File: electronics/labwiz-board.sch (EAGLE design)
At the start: 97 parts, among them J1 SD_MICRO_SDIO_1BIT, J2 CORTEX_DEBUGSMD_original, U1 STM32F10XRXT6, U2 MCP73831/2, U4 MIC5219-3.3V, X2 M12_BOTTOM_CONTACTS_FPC_1MM, Y3 32.768kHz

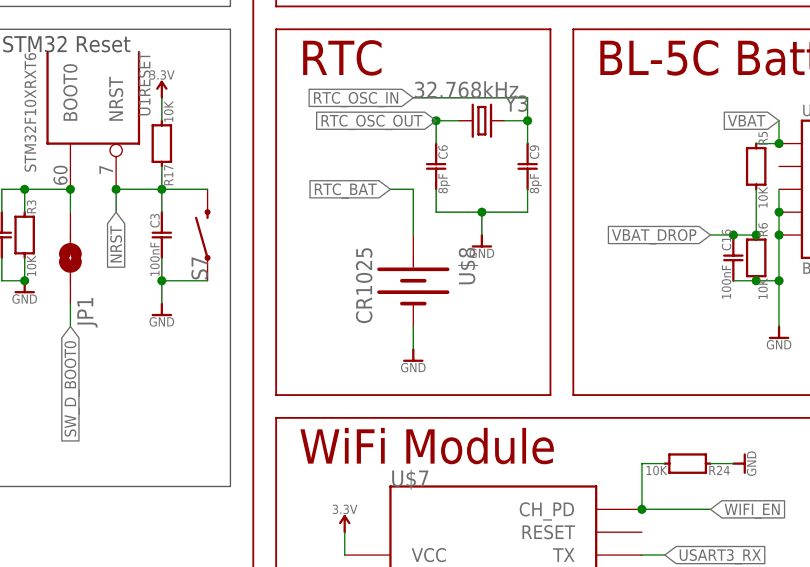
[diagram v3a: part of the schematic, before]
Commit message: Routed the RTC battery. Bumped a bunch of traces around.
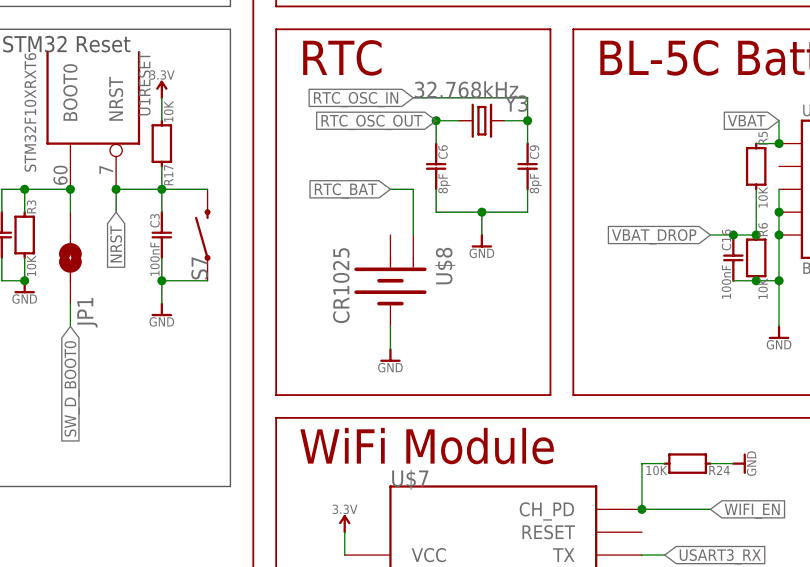
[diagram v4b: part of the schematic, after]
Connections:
- net RTC_BAT: now also U$8.+1; no longer U$8.+
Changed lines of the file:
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@@
 <instance part="C6" gate="G$1" x="132.08" y="73.66" rot="R180"/>
 <instance part="C9" gate="G$1" x="142.24" y="73.66" rot="R180"/>
-<instance part="GND5" gate="G$1" x="129.54" y="53.34"/>
+<instance part="GND5" gate="G$1" x="127" y="53.34"/>
 <instance part="U$2" gate="G$1" x="342.9" y="15.24"/>
 <instance part="R18" gate="G$1" x="269.24" y="25.4" rot="MR90"/>
@@
 <instance part="SUPPLY10" gate="G$1" x="121.92" y="33.02"/>
 <instance part="TP1" gate="G$1" x="116.84" y="27.94" rot="R180"/>
-<instance part="U$8" gate="G$1" x="129.54" y="60.96" rot="R270"/>
+<instance part="U$8" gate="G$1" x="127" y="60.96"/>
 </instances>
 <busses>
@@
 <pinref part="GND5" gate="G$1" pin="GND"/>
 <pinref part="U$8" gate="G$1" pin="-"/>
-<wire x1="129.54" y1="53.34" x2="129.54" y2="55.88" width="0.1524" layer="91"/>
+<wire x1="127" y1="53.34" x2="127" y2="55.88" width="0.1524" layer="91"/>
 </segment>
 <segment>
@@
 </segment>
 <segment>
-<wire x1="129.54" y1="66.04" x2="129.54" y2="71.12" width="0.1524" layer="91"/>
 <wire x1="129.54" y1="71.12" x2="127" y2="71.12" width="0.1524" layer="91"/>
-<pinref part="U$8" gate="G$1" pin="+"/>
-</segment>
-</net>
+<pinref part="U$8" gate="G$1" pin="+1"/>
+<wire x1="129.54" y1="71.12" x2="129.54" y2="66.04" width="0.1524" layer="91"/>
+</segment>
+</net>

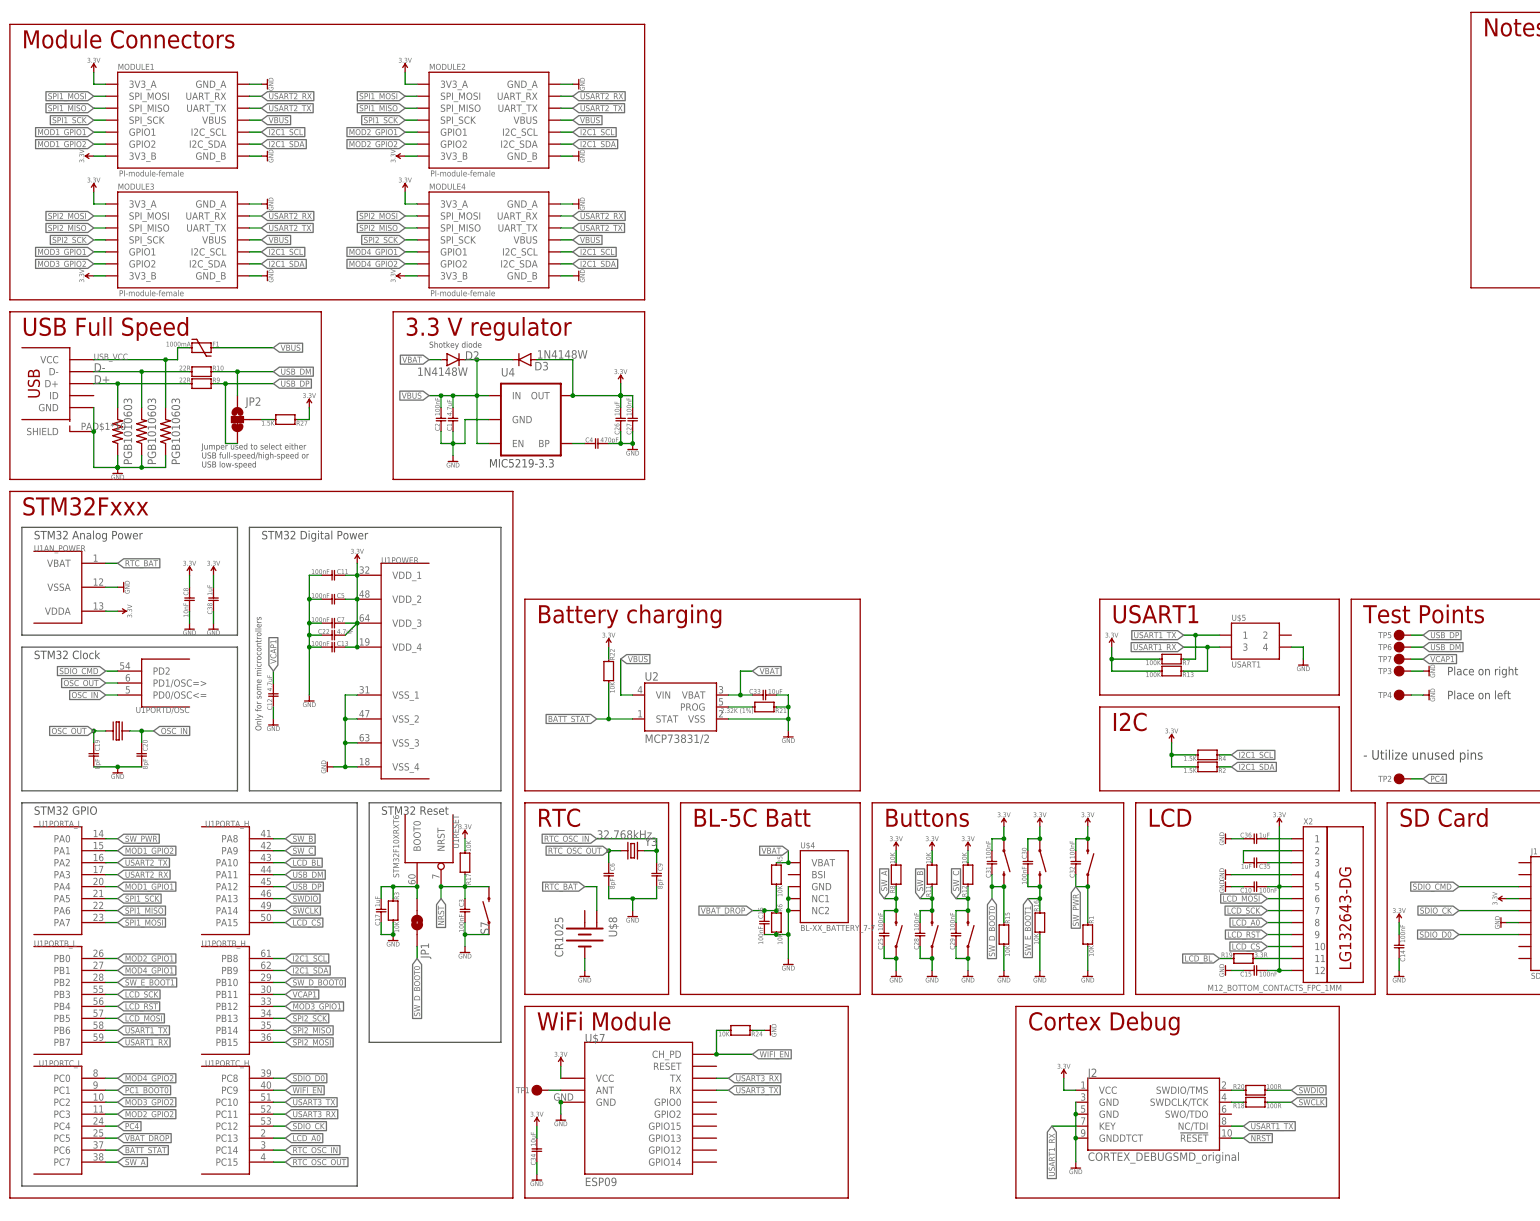
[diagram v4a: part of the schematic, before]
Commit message: PC4 is now VBUS_DETECT. Removed unnecessary USB data series resistors. Closes #76.'
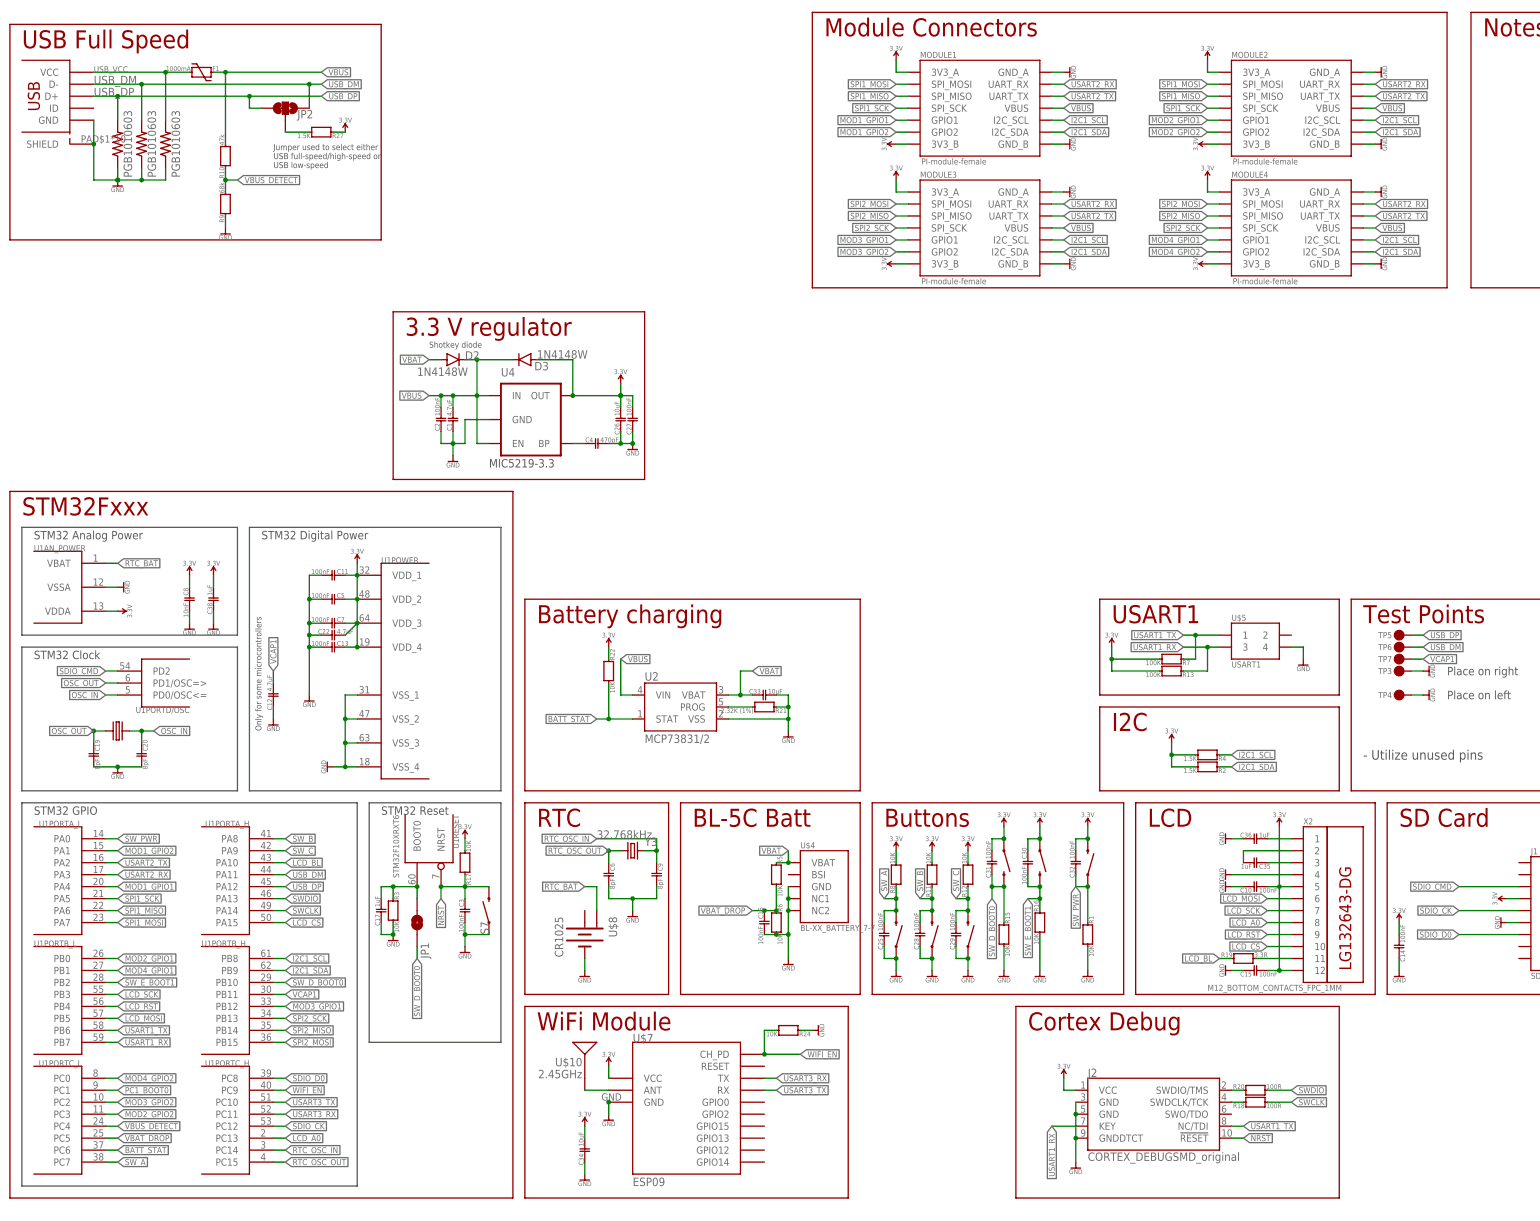
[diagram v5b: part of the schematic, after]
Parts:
- removed TP1, TP2: DNP, PaxInstruments-Connectors:M01_PAD_1MM
- added U$10: 2.45GHz, SparkFun-RF:ANTENNA2.4GHZ-6.5X2.2MM
- R10: value 22R -> 47k; device PaxInstruments-RCL:RESISTOR_FIXED_22R_0402 -> PaxInstruments-RCL:RESISTOR_FIXED_0402
- R9: value 22R -> 68k; device PaxInstruments-RCL:RESISTOR_FIXED_22R_0402 -> PaxInstruments-RCL:RESISTOR_FIXED_0402
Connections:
- removed net D+: R9.1, U$1.D+, Z1.2
- removed net D-: R10.1, U$1.D-, Z2.2
- removed net PC4: TP2.P$1, U1PORTC_L.PC4
- new net VBUS_DETECT: R10.2, R9.1, U1PORTC_L.PC4
- net GND: now also R9.2
- net N$13: now also U$10.SIGNAL; no longer TP1.P$1
- net USB_DM: now also U$1.D-, Z2.2; no longer R10.2
- net USB_DP: now also U$1.D+, Z1.2; no longer R9.2
- net VBUS: now also R10.1
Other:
- moved on the sheet: C34, F1, JP2, MODULE1, MODULE2, MODULE3, MODULE4, R10, R24, R27, R9, U$7

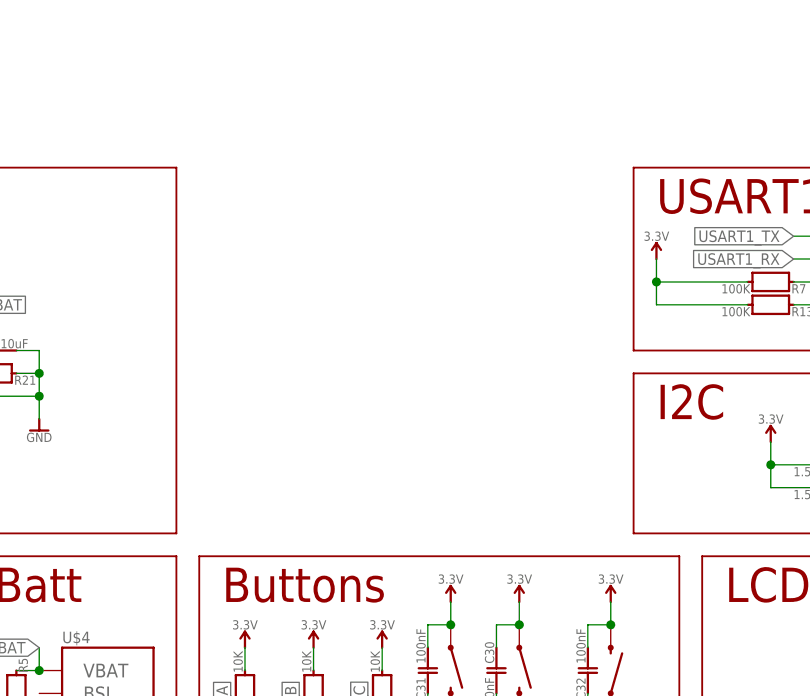
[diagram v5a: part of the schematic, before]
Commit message: Added SPI pullups. Need to route.
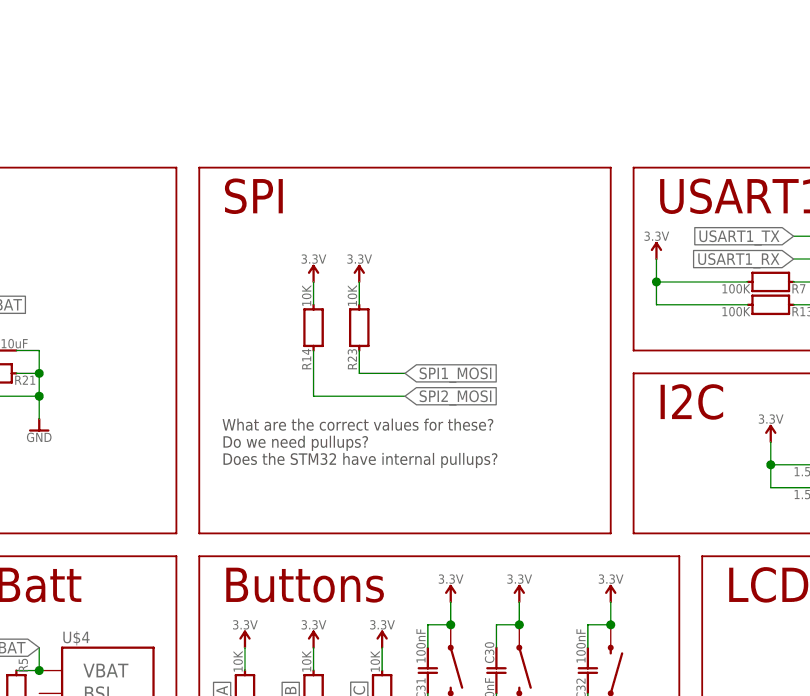
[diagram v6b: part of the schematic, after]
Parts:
- added R14, R23: 10K, PaxInstruments-RCL:RESISTOR_FIXED_10K_0402
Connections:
- net 3.3V: now also R14.1, R23.1
- net SPI1_MOSI: now also R23.2
- net SPI2_MOSI: now also R14.2
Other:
- note added: "SPI"
- note added: "What are the correct values for these? Do we need pullups? Does the STM32 have internal pullups?"
